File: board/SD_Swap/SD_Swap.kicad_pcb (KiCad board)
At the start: 2 copper layers, 33 x 27 mm, 42 parts, among them J1 USB_C, Q1 Q_Dual_PNP_PNP_E1B1C2E2B2C1, U1 74LVC2G14, U2 RTS5306E, U4 93AAxxAT, U5 TS3A27518ERTW, U7 AP2127N-3.3, Y1 12MHz

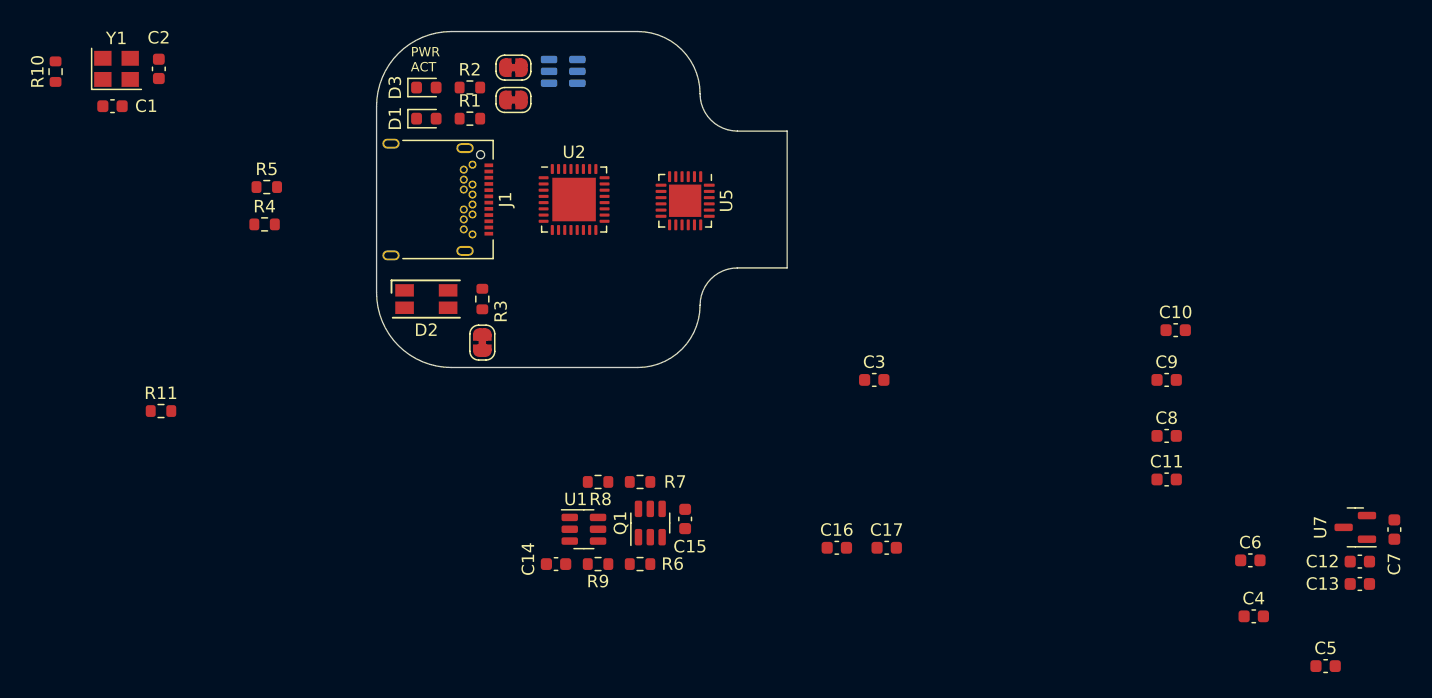
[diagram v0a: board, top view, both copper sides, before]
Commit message: mostly done with the usb side of the brd
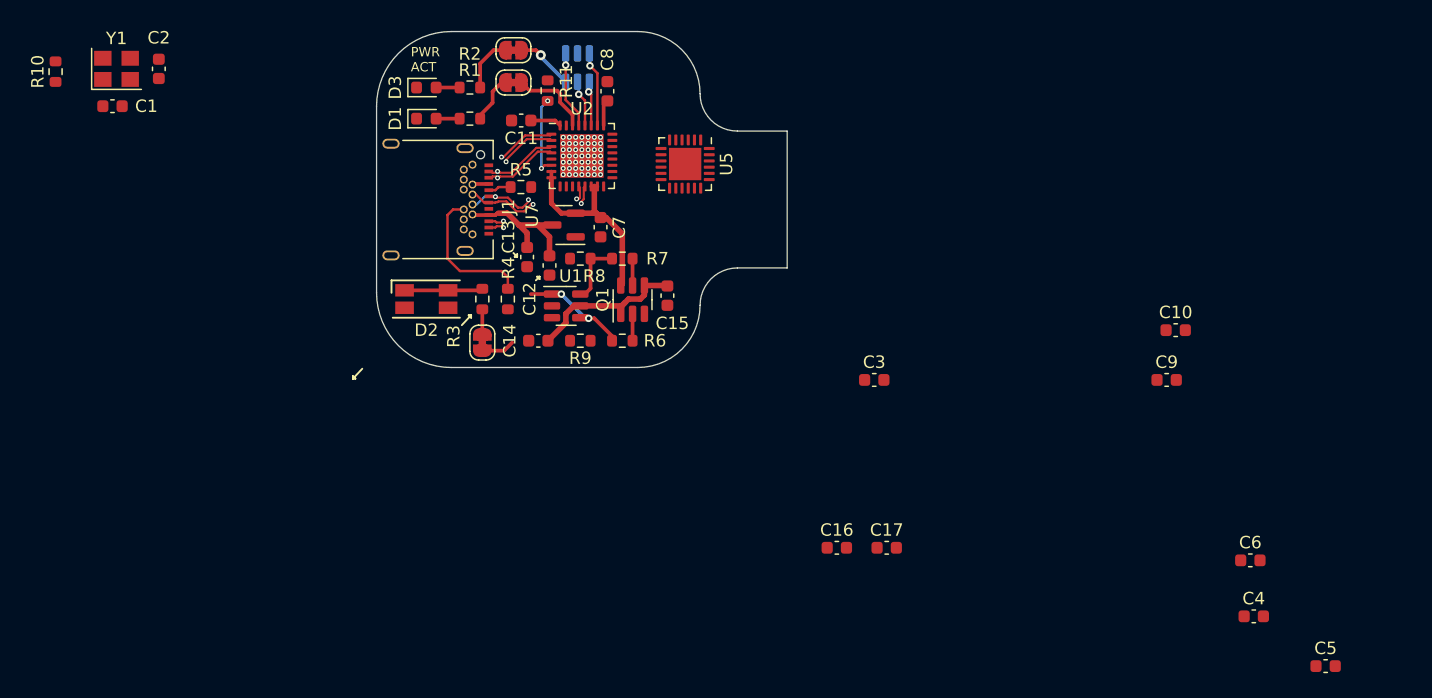
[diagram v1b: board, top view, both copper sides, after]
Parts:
- moved C13 71.9 mm to (103.1, 86.1), turned to -90 degrees
- moved C12 69.3 mm to (104.9, 86.8), turned to -90 degrees
- moved C7 68.3 mm to (109.0, 83.7)
- moved U7 68.1 mm to (106.1, 83.5)
- moved C11 59.4 mm to (102.6, 75.2), turned to 180 degrees
- moved C8 52.8 mm to (109.5, 72.8), turned to 90 degrees
- moved R11 40.4 mm to (104.8, 72.8), turned to 90 degrees
- moved R4 20.4 mm to (101.5, 89.5), turned to -90 degrees
- moved R5 20.4 mm to (102.6, 80.5)
- moved C14 18.0 mm to (104.0, 92.8)
- moved C15 18.0 mm to (114.4, 89.2)
- moved Q1 18.0 mm to (111.6, 89.5)
- moved R6 18.0 mm to (110.8, 92.8)
- moved R7 18.0 mm to (110.8, 86.2)
- moved R8 18.0 mm to (107.4, 86.2)
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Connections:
- U2 pad 14: +5V -> +3.3V
- U2 pad 8: +5V -> +3.3V
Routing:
- net +3.3V: track 0.00 -> 21.4 mm, vias 0 -> 1
- net /SS_RX+: track 0.00 -> 17.5 mm, vias 0 -> 2
- net /SS_RX-: track 0.00 -> 16.4 mm, vias 0 -> 2
- net VCC: track 0.00 -> 13.8 mm
- net /USB+: track 0.00 -> 13.6 mm, vias 0 -> 3
- net /SS_TX+: track 0.00 -> 13.2 mm, vias 0 -> 1
- net +5V: track 0.00 -> 13.2 mm
- net /SS_TX-: track 0.00 -> 12.4 mm, vias 0 -> 1
- net Net-(JP3-Pad2): track 0.00 -> 11.7 mm, vias 0 -> 2
- net /USB-: track 0.00 -> 11.5 mm, vias 0 -> 2
- net Net-(J1-PadB5): track 0.00 -> 11.4 mm
- net Net-(R11-Pad1): track 0.00 -> 6.54 mm, vias 0 -> 2
- net /ACT: track 0.00 -> 6.44 mm
- net Net-(D2-Pad1): track 0.00 -> 6.30 mm
- net Net-(U2-Pad29): track 0.00 -> 6.22 mm, vias 0 -> 1
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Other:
- copper layers 2 -> 4

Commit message: doing more brd
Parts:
- C1, C2, R10, Y1: moved to B.Cu
- moved R10 38.9 mm to (103.0, 80.5), turned to 180 degrees
- moved Y1 38.7 mm to (106.5, 84.2)
- moved C2 38.4 mm to (109.6, 84.2), turned to 90 degrees
- moved C1 35.1 mm to (103.4, 84.2), turned to -90 degrees
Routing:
- net VCC: track 13.8 -> 27.0 mm, vias 0 -> 2
- net +1V2: track 4.61 -> 16.9 mm, vias 0 -> 3
- net Net-(C2-Pad1): track 0.00 -> 7.57 mm, vias 0 -> 1
- net Net-(C1-Pad1): track 0.00 -> 7.20 mm, vias 0 -> 1
- net Net-(JP3-Pad2): track 11.7 -> 16.2 mm
- net Net-(R11-Pad1): track 6.54 -> 7.42 mm
- net GND: vias 49 -> 50
- added copper zone on In1.Cu, net +5V
- added copper zone on In2.Cu, net +5V
- added copper zone on B.Cu, net GND
- added copper zone on F.Cu, net GND
- added copper zone on In1.Cu, net GND
- added copper zone on In2.Cu, net GND

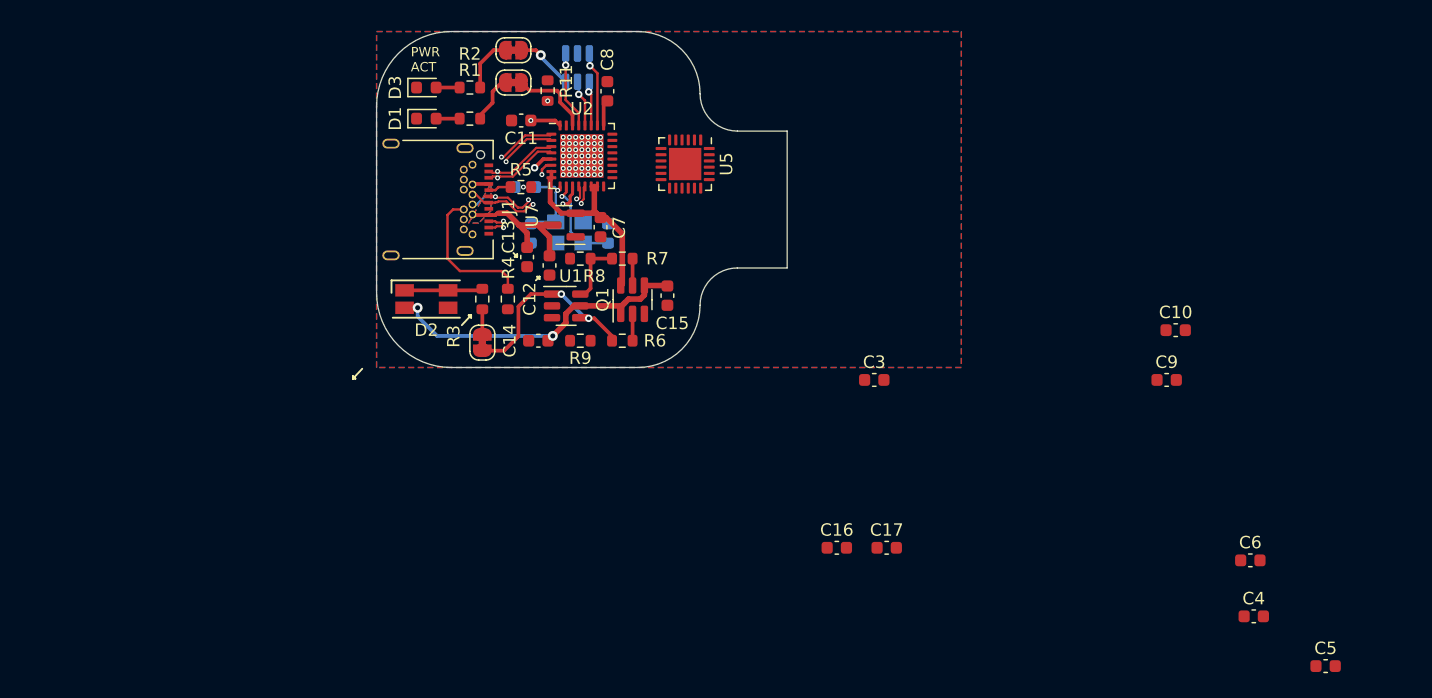
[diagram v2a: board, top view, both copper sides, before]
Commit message: add pcb-sd footprint add some notes in the sch
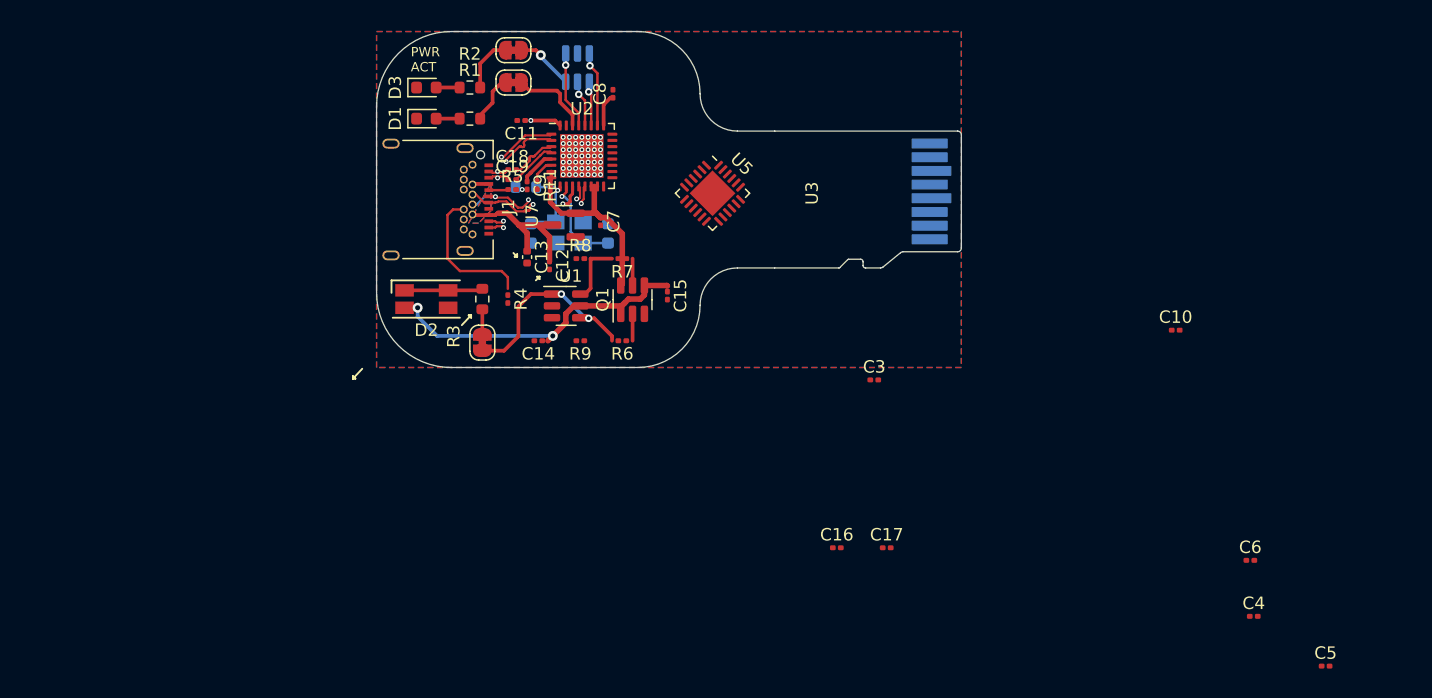
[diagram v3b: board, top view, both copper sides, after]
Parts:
- added C18: 0.1u, Capacitor_SMD:C_0201_0603Metric, F.Cu at (101.9, 79.1)
- added C19: 0.1u, Capacitor_SMD:C_0201_0603Metric, F.Cu at (101.9, 79.9)
- added U3: PCB_SD, SD_Swap:PCB-SD, F.Cu at (123.0, 76.0)
- C10, C11, C12, C14, C15, C16, C17, C3, C4, C5, C6, C7, C8, C9: footprint Capacitor_SMD:C_0603_1608Metric -> Capacitor_SMD:C_0201_0603Metric
- C13: footprint Capacitor_SMD:C_0603_1608Metric -> Capacitor_SMD:C_0402_1005Metric
- R11, R4, R5, R6, R7, R8, R9: footprint Resistor_SMD:R_0603_1608Metric -> Resistor_SMD:R_0201_0603Metric
- moved C9 53.7 mm to (103.1, 80.4), turned to -90 degrees
- moved R11 7.65 mm to (103.9, 80.4), turned to -90 degrees
- moved U5 3.22 mm to (118.0, 81.0), turned to -45 degrees
- moved R5 0.73 mm to (101.9, 80.7)
- moved C8 0.49 mm to (110.0, 73.0)
- moved C7 0.47 mm to (109.0, 83.3)
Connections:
- U2 pad 3: /SS_TX+ -> /SS_TXC+
- U2 pad 4: /SS_TX- -> /SS_TXC-
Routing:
- net Net-(R11-Pad1): track 7.42 -> 2.01 mm, vias 2 -> 0
- net /SS_TX+: track 13.2 -> 8.94 mm
- net /SS_TXC+: track 0.00 -> 4.11 mm
- net /SS_TXC-: track 0.00 -> 4.08 mm
- net /SS_TX-: track 12.4 -> 8.87 mm
- net +1V2: track 16.9 -> 18.7 mm, vias 3 -> 2
- net /SS_RX-: track 16.4 -> 17.6 mm
- net +5V: track 13.2 -> 13.9 mm
- net /USB-: track 11.5 -> 12.1 mm
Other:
- board size 33 x 27 mm -> 32 x 27 mm

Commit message: add board mostly done
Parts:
- moved C6 68.4 mm to (105.2, 71.2), turned to -90 degrees
- moved C5 67.0 mm to (110.4, 83.6)
- moved C4 60.5 mm to (110.4, 82.7)
- moved C10 49.2 mm to (107.1, 81.6), turned to 180 degrees
- moved C17 40.0 mm to (114.5, 73.5)
- moved C16 32.8 mm to (115.4, 79.2), turned to 90 degrees
- moved C3 24.4 mm to (112.2, 80.4), turned to -90 degrees
- moved R9 4.37 mm to (103.6, 90.7), turned to -90 degrees
- moved C7 3.45 mm to (105.8, 82.0)
- moved C11 2.93 mm to (105.4, 74.2)
- moved C14 2.58 mm to (106.5, 92.4), turned to 0 degrees
- moved R7 2.44 mm to (109.0, 87.9), turned to -90 degrees
- moved U7 2.05 mm to (106.0, 85.6)
- moved C12 1.86 mm to (103.2, 86.1)
- moved R4 1.60 mm to (101.0, 88.0)
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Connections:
- U5 pad 10: Net-(U2-Pad21) -> Net-(U2-Pad19)
- U5 pad 12: Net-(U2-Pad19) -> Net-(U2-Pad20)
- U5 pad 13: Net-(U2-Pad22) -> Net-(U2-Pad21)
- U5 pad 14: Net-(U2-Pad18) -> Net-(U2-Pad22)
- U5 pad 18: Net-(U3-Pad8) -> Net-(U3-Pad2)
- U5 pad 19: Net-(U3-Pad2) -> Net-(U3-Pad3)
- U5 pad 20: Net-(U3-Pad7) -> Net-(U3-Pad5)
- U5 pad 22: Net-(U3-Pad3) -> Net-(U3-Pad7)
- U5 pad 23: Net-(U3-Pad5) -> Net-(U3-Pad8)
- U5 pad 8: Net-(U2-Pad20) -> Net-(U2-Pad18)
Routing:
- net +3.3V: track 21.4 -> 43.1 mm, vias 1 -> 4
- net Net-(R9-Pad2): track 0.00 -> 20.6 mm, vias 0 -> 2
- net Net-(U3-Pad1): track 0.00 -> 17.7 mm, vias 0 -> 2
- net Net-(U3-Pad8): track 0.00 -> 17.7 mm, vias 0 -> 2
- net Net-(U3-Pad2): track 0.00 -> 17.6 mm, vias 0 -> 2
- net Net-(U3-Pad3): track 0.00 -> 17.6 mm, vias 0 -> 2
- net Net-(U3-Pad5): track 0.00 -> 17.6 mm, vias 0 -> 2
- net Net-(U3-Pad7): track 0.00 -> 17.6 mm, vias 0 -> 2
- net Net-(U2-Pad23): track 0.00 -> 12.9 mm, vias 0 -> 2
- net Net-(U2-Pad22): track 0.00 -> 11.7 mm, vias 0 -> 2
- net Net-(U2-Pad21): track 0.00 -> 10.5 mm, vias 0 -> 2
- net Net-(U2-Pad20): track 0.00 -> 10.1 mm, vias 0 -> 2
- net /SD_SEL: track 5.14 -> 14.6 mm
- net Net-(U2-Pad19): track 0.00 -> 8.51 mm, vias 0 -> 2
- net Net-(U2-Pad18): track 0.00 -> 6.89 mm, vias 0 -> 2
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- added copper zone on In1.Cu, net Net-(U3-Pad4)
- added copper zone on In2.Cu, net VCC
- removed copper zone on In1.Cu, net GND
- removed copper zone on In2.Cu, net GND
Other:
- board text added: "Need to redo usb3 spacing is wrong"
- board text added: "UHS50 cards must have 50ohm nominal impedance. There is no length matich requirements but so 0.5mm is ok."

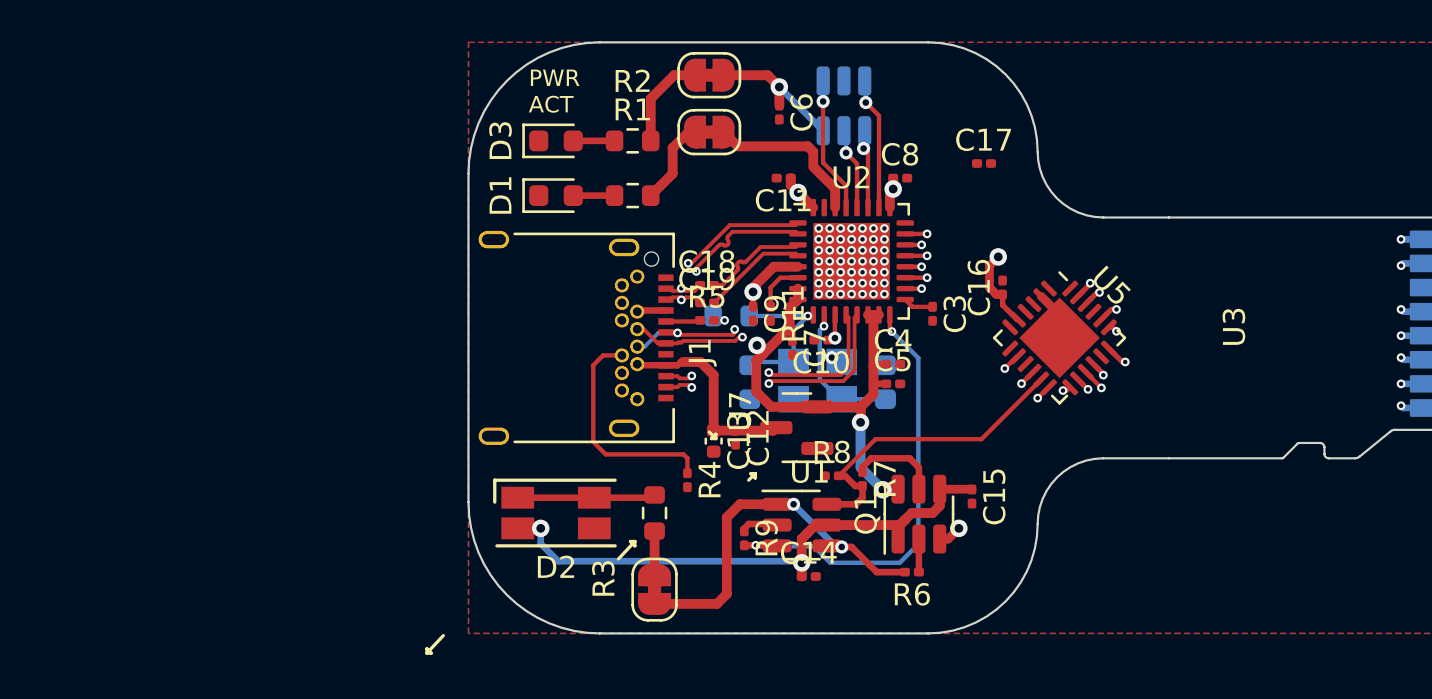
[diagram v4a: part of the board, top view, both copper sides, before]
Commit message: add sdcard holder
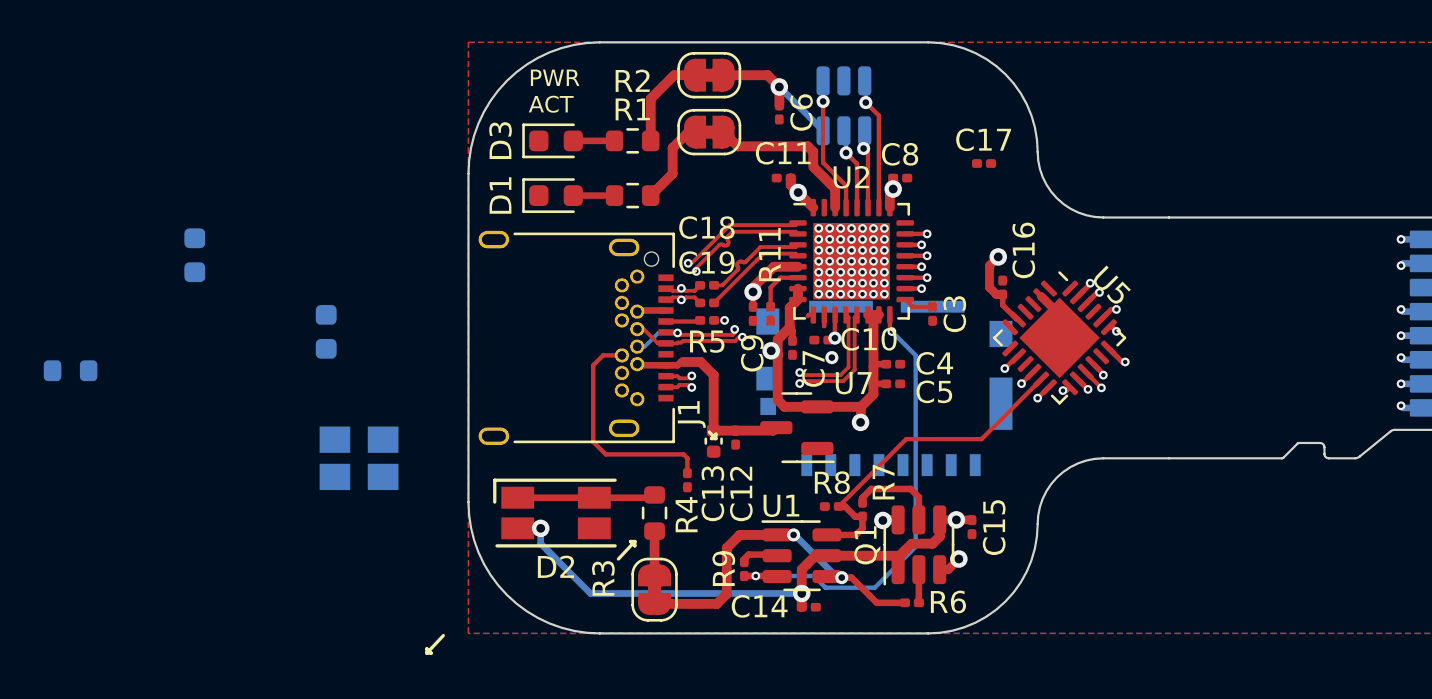
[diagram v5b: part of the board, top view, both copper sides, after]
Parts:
- added U6: SD_SOCKET, SD_Swap:105162-0001, B.Cu at (110.0, 80.0)
- moved R10 30.3 mm to (72.8, 83.0)
- moved C1 26.0 mm to (78.5, 77.7)
- moved C2 25.7 mm to (84.5, 81.2)
- moved Y1 21.2 mm to (86.0, 87.0)
- moved Q1 1.40 mm to (111.6, 91.0)
- moved R7 1.40 mm to (109.0, 89.3)
- moved R8 1.40 mm to (107.6, 89.2)
- moved R9 1.40 mm to (103.6, 92.1)
- moved U1 1.40 mm to (106.2, 91.5)
- moved C14 1.40 mm to (106.5, 93.8)
- moved C15 1.40 mm to (114.0, 90.1)
- moved R6 1.40 mm to (111.3, 93.6)
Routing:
- net Net-(C1-Pad1): track 7.16 -> 0.27 mm, vias 1 -> 0
- net Net-(C2-Pad1): track 6.31 -> 0.52 mm, vias 1 -> 0
- net +3.3V: track 43.1 -> 38.7 mm
- net Net-(JP3-Pad2): track 17.3 -> 15.9 mm
- net VCC: track 30.1 -> 31.4 mm, vias 3 -> 4
- net /SD_SEL: track 14.6 -> 15.2 mm

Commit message: more routing
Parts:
- moved C16 0.86 mm to (115.1, 80.0), turned to 180 degrees
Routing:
- net Net-(U5-Pad4): track 0.00 -> 16.3 mm, vias 0 -> 2
- net Net-(U5-Pad6): track 0.00 -> 13.2 mm, vias 0 -> 2
- net Net-(U5-Pad7): track 0.00 -> 12.9 mm, vias 0 -> 2
- net Net-(U5-Pad3): track 0.00 -> 12.3 mm, vias 0 -> 2
- net Net-(U5-Pad1): track 0.00 -> 12.1 mm, vias 0 -> 2
- net Net-(U5-Pad9): track 0.00 -> 10.9 mm, vias 0 -> 2
- net +3.3V: track 38.7 -> 49.3 mm, vias 4 -> 3
- net VCC: track 31.4 -> 35.4 mm
- net /SD_SEL: track 15.2 -> 15.8 mm
- net Net-(R9-Pad2): track 20.9 -> 20.3 mm
- net Net-(Q1-Pad5): track 4.16 -> 3.62 mm
- net GND: vias 51 -> 85
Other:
- board text added: "Need to redo usb3 spacing is wrong Length mathicng on sdio"
- board text removed: "Need to redo usb3 spacing is wrong"
